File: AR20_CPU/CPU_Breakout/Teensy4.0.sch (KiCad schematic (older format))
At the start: 15 parts, among them SW1 SW_SPST

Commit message: E
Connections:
- net 22_CTX1 is gone; now on net Out1: Teensy4.0.10 (22_A8)
- net 23_CRX1 is gone; now on net Out2: Teensy4.0.8 (23_A9)
- net 26_A12: now also D9.1 (K), OpAmp1.3 (IN-), OpAmp1.4 (OUT); no longer MX1.43 (Pin_43)
- net 30_CRX3: no longer MX1.39 (Pin_39)
- net 31_CTX3: no longer MX1.37 (Pin_37)
- net Ground: now also MX1.43 (Pin_43)
- net Out1: no longer Teensy4.0.14 (20_A6_TX5)
- net Out2: no longer Teensy4.0.12 (21_A7_RX5)
- removed net 24_A10: D9.1 (K), MX1.22 (Pin_22), OpAmp1.3 (IN-), OpAmp1.4 (OUT), Teensy4.0.38 (24_A10_TX6)
- net 25_A11 renamed 25_RX6_A11
- net 8_IN1 renamed 8_TX2_IN1
- new net 20_TX5: MX1.39 (Pin_39), Teensy4.0.14 (20_A6_TX5)
- new net 21_RX5: MX1.37 (Pin_37), Teensy4.0.12 (21_A7_RX5)
- new net 24_TX6_A10: MX1.22 (Pin_22), Teensy4.0.38 (24_A10_TX6)
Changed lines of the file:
@@
 Text GLabel 9550 3500 2    50   Input ~ 0
 Out3
-Text GLabel 9550 3400 2    50   Input ~ 0
+Text GLabel 9550 3200 2    50   Input ~ 0
 Out1
-Text GLabel 9550 3300 2    50   Input ~ 0
+Text GLabel 9550 3100 2    50   Input ~ 0
 Out2
 Text GLabel 9550 3600 2    50   Input ~ 0
@@
 26_A12
 Text GLabel 9550 4600 2    50   Input ~ 0
-24_A10
+24_TX6_A10
 Text GLabel 9550 4200 2    50   Input ~ 0
 3V3
@@
 Text GLabel 9550 2800 2    50   Input ~ 0
 Vinn_5V
-Text GLabel 9550 3100 2    50   Input ~ 0
-23_CRX1
-Text GLabel 9550 3200 2    50   Input ~ 0
-22_CTX1
+Text GLabel 9550 3300 2    50   Input ~ 0
+21_RX5
+Text GLabel 9550 3400 2    50   Input ~ 0
+20_TX5
 $Comp
 L BreakoutBoardTeensy:Teensy_pins Teensy4.?
@@
 27_A13
 Text GLabel 7200 4900 0    50   Input ~ 0
-25_A11
+25_RX6_A11
 Text GLabel 7200 3800 0    50   Input ~ 0
 9_OUT1C
 Text GLabel 7200 3700 0    50   Input ~ 0
-8_IN1
+8_TX2_IN1
 Text GLabel 7200 3600 0    50   Input ~ 0
 7_RX2_OUT1A
@@
 Wire Wire Line
 	4600 3900 4500 3900
-Text GLabel 4500 3900 0    50   Input ~ 0
-24_A10
-Text GLabel 4400 5200 0    50   Input ~ 0
-26_A12
 Text GLabel 4400 4500 0    50   Input ~ 0
 28_RX7
 Text GLabel 4400 5000 0    50   Input ~ 0
 33_MCLK2
-Text GLabel 4400 4600 0    50   Input ~ 0
-31_CTX3
 Text GLabel 4400 5100 0    50   Input ~ 0
 29_TX7
 Text GLabel 4400 4700 0    50   Input ~ 0
 27_A13
-Text GLabel 4400 4000 0    50   Input ~ 0
-25_A11
 Text GLabel 4500 3600 0    50   Input ~ 0
 9_OUT1C
-Text GLabel 4500 3500 0    50   Input ~ 0
-8_IN1
 Text GLabel 4500 3400 0    50   Input ~ 0
 7_RX2_OUT1A
@@
 Wire Wire Line
 	4600 5800 4400 5800
-Text GLabel 4400 4800 0    50   Input ~ 0
-30_CRX3
 Text GLabel 4400 4900 0    50   Input ~ 0
 32_OUT1B
@@
 Wire Wire Line
 	9050 1250 8900 1250
-Text GLabel 7600 1700 0    50   Input ~ 0
-24_A10
 $Comp
 L Device:C C19
@@
 Wire Wire Line
 	7700 1700 7750 1700
-Wire Wire Line
-	10550 2050 10550 2000
-Wire Wire Line
-	10550 2400 10550 2350
 $Comp
 L Device:D_Zener D?
@@
 Wire Wire Line
 	7800 2400 7800 2250
+Text GLabel 4400 4600 0    50   Input ~ 0
+21_RX5
+Text GLabel 4400 4800 0    50   Input ~ 0
+20_TX5
+Text GLabel 4500 3500 0    50   Input ~ 0
+8_TX2_IN1
+Text GLabel 4400 4000 0    50   Input ~ 0
+25_RX6_A11
+Text GLabel 4500 3900 0    50   Input ~ 0
+24_TX6_A10
+Text GLabel 4400 5200 0    50   Input ~ 0
+Ground
+Text GLabel 7600 1700 0    50   Input ~ 0
+26_A12
+Wire Wire Line
+	7800 1700 7700 1700
 $EndSCHEMATC

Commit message: E2
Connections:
- net 3V3 is gone; now on net 3.3V: MX1.21 (Pin_21), Teensy4.0.30 (3V3)
- net 3.3V: no longer MX1.20 (Pin_20)
- net Ground: now also MX1.20 (Pin_20)
- net IN+: now also C19.1, R21.2, R22.1; no longer JP10.1 (A)
- net VBAT: now also JP10.2 (B); no longer R21.1
- new net: JP10.1 (A), R21.1
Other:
- moved on the sheet: C19, JP10, R21, R22
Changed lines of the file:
@@
 Text GLabel 9550 4600 2    50   Input ~ 0
 24_TX6_A10
-Text GLabel 9550 4200 2    50   Input ~ 0
+Text GLabel 10200 4200 2    50   Input ~ 0
 3V3
 Text GLabel 9550 3000 2    50   Input ~ 0
@@
 	9450 4000 9550 4000
 Wire Wire Line
-	9450 4200 9550 4200
-Wire Wire Line
 	9450 4300 9550 4300
 Wire Wire Line
@@
 	4600 3600 4500 3600
 Wire Wire Line
-	4600 3700 4500 3700
-Wire Wire Line
-	4600 3800 4500 3800
-Wire Wire Line
 	4600 3900 4500 3900
 Text GLabel 4400 4500 0    50   Input ~ 0
@@
 Text GLabel 4400 4900 0    50   Input ~ 0
 32_OUT1B
-Text GLabel 4500 3800 0    50   Input ~ 0
+Text GLabel 4300 3800 0    50   Input ~ 0
 3V3
 Wire Wire Line
@@
 Text GLabel 4400 4400 0    50   Input ~ 0
 Ground
-Text GLabel 4500 3700 0    50   Input ~ 0
-3.3V
 $Comp
 L Device:R R21
 U 1 1 5DE96DA3
-P 9750 1100
-F 0 "R21" H 9820 1146 50  0000 L CNN
-F 1 "?" H 9820 1055 50  0000 L CNN
-F 2 "Resistor_SMD:R_0603_1608Metric" V 9680 1100 50  0001 C CNN
-F 3 "~" H 9750 1100 50  0001 C CNN
-	1    9750 1100
+P 9450 1100
+F 0 "R21" H 9520 1146 50  0000 L CNN
+F 1 "?" H 9520 1055 50  0000 L CNN
+F 2 "Resistor_SMD:R_0603_1608Metric" V 9380 1100 50  0001 C CNN
+F 3 "~" H 9450 1100 50  0001 C CNN
+	1    9450 1100
 	1    0    0    -1
 $EndComp
@@
 L Device:R R22
 U 1 1 5DE9741A
-P 9750 1450
-F 0 "R22" H 9820 1496 50  0000 L CNN
-F 1 "?" H 9820 1405 50  0000 L CNN
-F 2 "Resistor_SMD:R_0603_1608Metric" V 9680 1450 50  0001 C CNN
-F 3 "~" H 9750 1450 50  0001 C CNN
-	1    9750 1450
+P 9450 1450
+F 0 "R22" H 9520 1496 50  0000 L CNN
+F 1 "?" H 9520 1405 50  0000 L CNN
+F 2 "Resistor_SMD:R_0603_1608Metric" V 9380 1450 50  0001 C CNN
+F 3 "~" H 9450 1450 50  0001 C CNN
+	1    9450 1450
 	1    0    0    -1
 $EndComp
 Wire Wire Line
-	10150 1150 10150 950
+	9450 1300 9450 1250
 Wire Wire Line
-	10150 1450 10150 1600
-Wire Wire Line
-	9750 1300 9750 1250
-Wire Wire Line
-	9750 950  10150 950
-Connection ~ 10150 950
-Wire Wire Line
-	10150 950  10150 900
-Wire Wire Line
-	9750 1600 10150 1600
-Connection ~ 10150 1600
-Wire Wire Line
-	10150 1600 10150 1650
-Connection ~ 9750 1250
+	9450 950  9850 950
+Connection ~ 9450 1250
 $Comp
 L Jumper:SolderJumper_2_Open JP10
 U 1 1 5DEBD2EA
-P 9200 1250
-F 0 "JP10" H 9200 1350 50  0000 C CNN
-F 1 "SolderJumper_2_Open" H 9250 1400 50  0000 C CNN
-F 2 "Jumper:SolderJumper-2_P1.3mm_Open_RoundedPad1.0x1.5mm" H 9200 1250 50  0001 C CNN
-F 3 "~" H 9200 1250 50  0001 C CNN
-	1    9200 1250
+P 10000 950
+F 0 "JP10" H 10000 1050 50  0000 C CNN
+F 1 "SolderJumper_2_Open" H 10050 1100 50  0000 C CNN
+F 2 "Jumper:SolderJumper-2_P1.3mm_Open_RoundedPad1.0x1.5mm" H 10000 950 50  0001 C CNN
+F 3 "~" H 10000 950 50  0001 C CNN
+	1    10000 950
 	1    0    0    -1
 $EndComp
-Wire Wire Line
-	9050 1250 8900 1250
 $Comp
 L Device:C C19
 U 1 1 5DEC35AF
-P 9500 1450
-F 0 "C19" H 9250 1500 50  0000 L CNN
-F 1 "?" H 9250 1350 50  0000 L CNN
-F 2 "Capacitor_SMD:C_0603_1608Metric" H 9538 1300 50  0001 C CNN
-F 3 "~" H 9500 1450 50  0001 C CNN
-	1    9500 1450
+P 9200 1450
+F 0 "C19" H 8950 1500 50  0000 L CNN
+F 1 "?" H 8950 1350 50  0000 L CNN
+F 2 "Capacitor_SMD:C_0603_1608Metric" H 9238 1300 50  0001 C CNN
+F 3 "~" H 9200 1450 50  0001 C CNN
+	1    9200 1450
 	1    0    0    -1
 $EndComp
 Wire Wire Line
-	9500 1300 9500 1250
-Connection ~ 9500 1250
-Wire Wire Line
-	9500 1250 9350 1250
+	9200 1300 9200 1250
+Connection ~ 9200 1250
 Wire Wire Line
-	9500 1250 9750 1250
-Text GLabel 9500 1650 3    50   Input ~ 0
+	9200 1250 9450 1250
+Text GLabel 9200 1650 3    50   Input ~ 0
 Ground
 Wire Wire Line
-	9500 1600 9500 1650
+	9200 1600 9200 1650
 Text GLabel 8950 900  1    50   Input ~ 0
 Vinn_5V
@@
 Wire Wire Line
 	7800 1700 7700 1700
+Wire Wire Line
+	4300 3800 4600 3800
+Text GLabel 4450 3700 0    50   Input ~ 0
+Ground
+Wire Wire Line
+	4450 3700 4600 3700
+Wire Wire Line
+	10150 900  10150 950
+Wire Wire Line
+	10150 1450 10150 1600
+Wire Wire Line
+	8900 1250 9200 1250
+Connection ~ 10150 950
+Wire Wire Line
+	10150 950  10150 1150
+Wire Wire Line
+	9450 1600 10150 1600
+Connection ~ 10150 1600
+Wire Wire Line
+	10150 1600 10150 1650
+Text GLabel 10050 4200 1    50   Input ~ 0
+3.3V
+Wire Wire Line
+	9450 4200 10200 4200
 $EndSCHEMATC

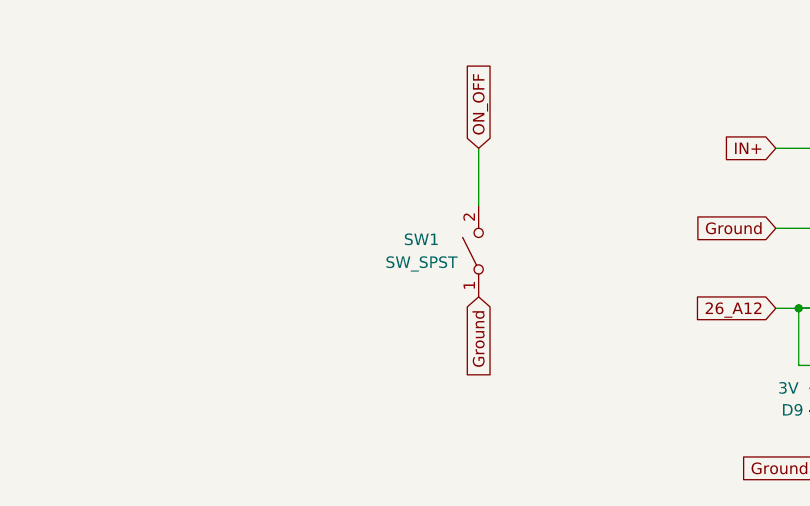
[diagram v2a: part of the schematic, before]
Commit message: Fixed push button
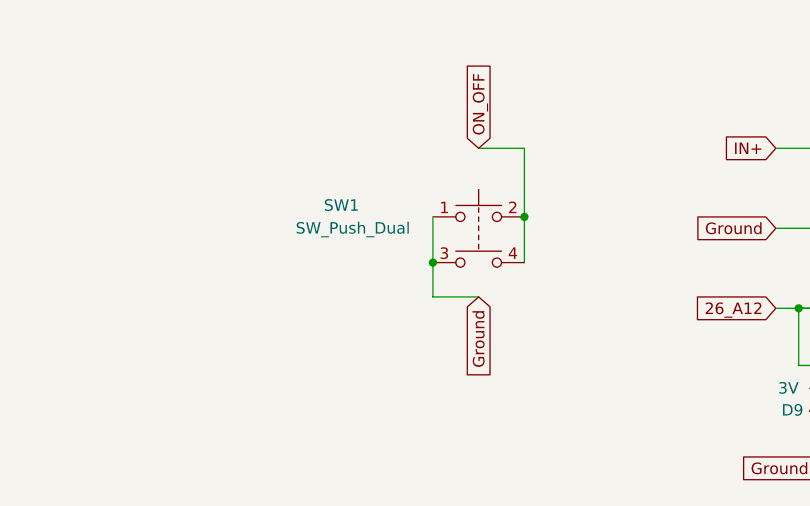
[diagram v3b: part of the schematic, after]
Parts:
- removed SW1: SW_SPST, Button_Switch_SMD:SW_DIP_SPSTx01_Slide_6.7x4.1mm_W6.73mm_P2.54mm_LowProfile_JPin, symbol Switch:SW_SPST
- added SW1: SW_Push_Dual, Button_Switch_SMD:SW_SPST_B3S-1000, symbol Switch:SW_Push_Dual
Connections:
- net Ground: now also SW1.1, SW1.3
- net ON_OFF: now also SW1.2, SW1.4
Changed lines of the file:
@@
 	1    0    0    -1
 $EndComp
-$Comp
-L Switch:SW_SPST SW1
-U 1 1 5DFDECE5
-P 6300 1450
-F 0 "SW1" V 6350 1700 50  0000 C CNN
-F 1 "SW_SPST" V 6250 1700 50  0000 C CNN
-F 2 "Button_Switch_SMD:SW_DIP_SPSTx01_Slide_6.7x4.1mm_W6.73mm_P2.54mm_LowProfile_JPin" H 6300 1450 50  0001 C CNN
-F 3 "~" H 6300 1450 50  0001 C CNN
-	1    6300 1450
-	0    -1   -1   0
-$EndComp
 Text GLabel 6300 1650 3    50   Input ~ 0
 Ground
 Text GLabel 6300 1000 1    50   Input ~ 0
 ON_OFF
-Wire Wire Line
-	6300 1250 6300 1000
 Text GLabel 10150 900  1    50   Input ~ 0
 VBAT
@@
 Wire Wire Line
 	9450 4200 10200 4200
+$Comp
+L Switch:SW_Push_Dual SW1
+U 1 1 5E1C0144
+P 6300 1300
+F 0 "SW1" H 5700 1350 50  0000 C CNN
+F 1 "SW_Push_Dual" H 5750 1250 50  0000 C CNN
+F 2 "Button_Switch_SMD:SW_SPST_B3S-1000" H 6300 1500 50  0001 C CNN
+F 3 "~" H 6300 1500 50  0001 C CNN
+	1    6300 1300
+	1    0    0    -1
+$EndComp
+Wire Wire Line
+	6100 1650 6300 1650
+Wire Wire Line
+	6100 1500 6100 1650
+Wire Wire Line
+	6500 1000 6500 1300
+Wire Wire Line
+	6300 1000 6500 1000
+Connection ~ 6100 1500
+Wire Wire Line
+	6100 1300 6100 1500
+Connection ~ 6500 1300
+Wire Wire Line
+	6500 1300 6500 1500
 $EndSCHEMATC

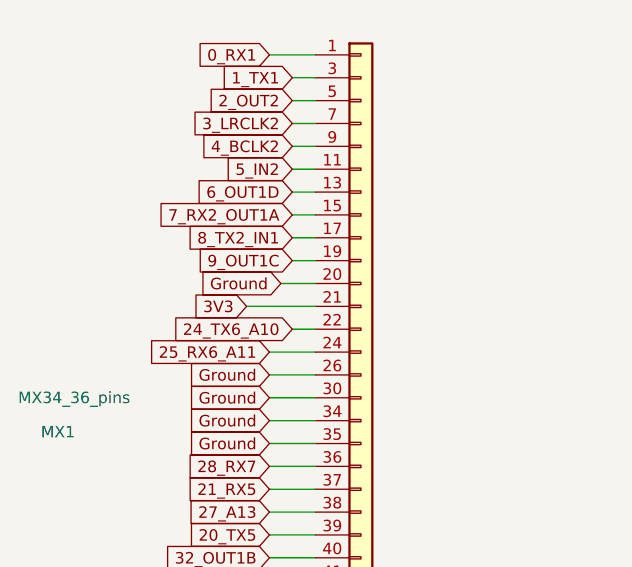
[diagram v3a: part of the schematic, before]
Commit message: Added 5V pin
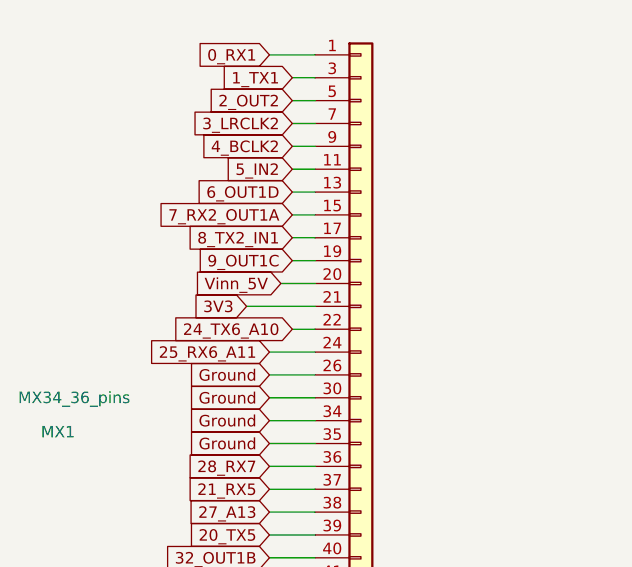
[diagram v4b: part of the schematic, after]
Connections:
- net Ground: no longer MX1.20 (Pin_20)
- net Vinn_5V: now also MX1.20 (Pin_20)
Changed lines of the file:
@@
 Wire Wire Line
 	4300 3800 4600 3800
-Text GLabel 4450 3700 0    50   Input ~ 0
-Ground
 Wire Wire Line
 	4450 3700 4600 3700
@@
 Wire Wire Line
 	6500 1300 6500 1500
+Text GLabel 4450 3700 0    50   Input ~ 0
+Vinn_5V
 $EndSCHEMATC
